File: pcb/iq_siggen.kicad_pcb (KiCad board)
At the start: 4 copper layers, 305 parts, among them J1 J3 - BANK0, J11 Conn_Coaxial, J12 Conn_01x01_Male, J13 Conn_01x01_Male, J14 Conn_01x01_Male, J15 Conn_01x01_Male, J16 Conn_01x01_Male, J17 Conn_01x01_Male, J18 Conn_Coaxial, J19 Conn_Coaxial, J2 J4 - BANK1, J3 Conn_01x10_Male, J4 Conn_01x01_Male, J5 Conn_01x10_Male, J6 Conn_Coaxial, J7 Conn_Coaxial, J8 Conn_Coaxial, J9 Conn_Coaxial, T1 Transformer_1P_SS, T2 Transformer_1P_SS, T3 Transformer_1P_SS, T4 Transformer_1P_SS, U1 AMS1117-3.3, U2 TPS72325DBVR, U3 TLV73325PDBVT, U4 TLV3542IDR, U5 LM2596S-ADJ, U6 MAX5853ETL-T, U7 TLV3542IDR

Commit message: routing mixer
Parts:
- moved D7 130.5 mm to (156.2, 257.8), turned to 180 degrees
- moved T1 122.7 mm to (150.5, 257.8), turned to 180 degrees
- moved T3 121.0 mm to (158.8, 250.2), turned to 90 degrees
- moved U4 120.3 mm to (127.6, 246.4)
- moved J12 120.0 mm to (76.8, 77.5)
- moved J17 118.8 mm to (64.8, 78.1)
- moved R25 111.3 mm to (260.3, 61.6)
- moved TP1 110.3 mm to (267.6, 63.1)
- moved J13 109.3 mm to (60.6, 70.5)
- moved J14 109.3 mm to (56.0, 70.5)
- moved J15 109.3 mm to (65.3, 70.5)
- moved D5 108.6 mm to (161.3, 257.8)
- moved R53 108.5 mm to (245.7, 56.5)
- moved U3 108.1 mm to (240.8, 57.6)
- moved R59 108.0 mm to (252.3, 59.1)
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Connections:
- T4 pad 1: GNDA -> /mixer/RF_I
- T4 pad 2: /mixer/RF_I -> GNDA
- T4 pad 3: Net-(D6-Pad3) -> Net-(D8-Pad3)
- T4 pad 5: Net-(D8-Pad3) -> Net-(D6-Pad3)
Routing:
- net Net-(D5-Pad2): track 0.00 -> 7.52 mm
- net Net-(D5-Pad1): track 0.00 -> 7.52 mm
- net Net-(D6-Pad2): track 0.00 -> 7.52 mm
- net Net-(D6-Pad1): track 0.00 -> 7.52 mm
- net Net-(D8-Pad3): track 0.00 -> 6.71 mm, vias 0 -> 1
- net Net-(D7-Pad3): track 0.00 -> 6.71 mm, vias 0 -> 1
- net Net-(D6-Pad3): track 0.00 -> 6.71 mm, vias 0 -> 1
- net Net-(D5-Pad3): track 0.00 -> 6.71 mm, vias 0 -> 1
- added copper zone on In1.Cu, net GNDA
- added copper zone on In2.Cu, net GNDA
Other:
- net class 100ohm differential added: clearance 0.1, trace_width 0.117094, via_dia 0.8, via_drill 0.4
- net class 50ohm single ended added: clearance 0.1, trace_width 0.146812, via_dia 0.8, via_drill 0.4
- net class Default: clearance 0.2 -> 0.1
- rule trace_clearance: 0.2 -> 0.1
- rule trace_min: 0.13 -> 0.1
- rule via_min_drill: 0.25 -> 0.23

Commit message: lined up data bus resistors, done 5v reg, started the -5V switching regulator
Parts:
- moved R65 202.3 mm to (181.0, 245.3), turned to 270 degrees
- moved R64 196.4 mm to (176.7, 244.5)
- moved C1 195.2 mm to (187.3, 244.5)
- moved R60 194.8 mm to (167.0, 248.3), turned to 270 degrees
- moved R62 190.0 mm to (171.6, 242.6), turned to 180 degrees
- moved R24 176.4 mm to (91.4, 83.2), turned to 90 degrees
- moved R63 171.3 mm to (171.6, 247.0), turned to 180 degrees
- moved R61 169.7 mm to (167.0, 241.7), turned to 90 degrees
- moved R40 162.4 mm to (88.9, 83.2), turned to 270 degrees
- moved R38 158.7 mm to (99.1, 83.2), turned to 270 degrees
- moved J11 141.7 mm to (212.1, 244.7)
- moved R44 141.6 mm to (116.8, 83.4), turned to 270 degrees
- moved R23 141.1 mm to (94.0, 83.2), turned to 90 degrees
- moved R36 140.3 mm to (106.7, 83.2), turned to 270 degrees
- moved R22 139.8 mm to (96.5, 83.2), turned to 90 degrees
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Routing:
- net +3V3: track 0.00 -> 16.5 mm
- net +5V: track 0.00 -> 3.42 mm
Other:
- net class Default: trace_width 0.25 -> 0.1

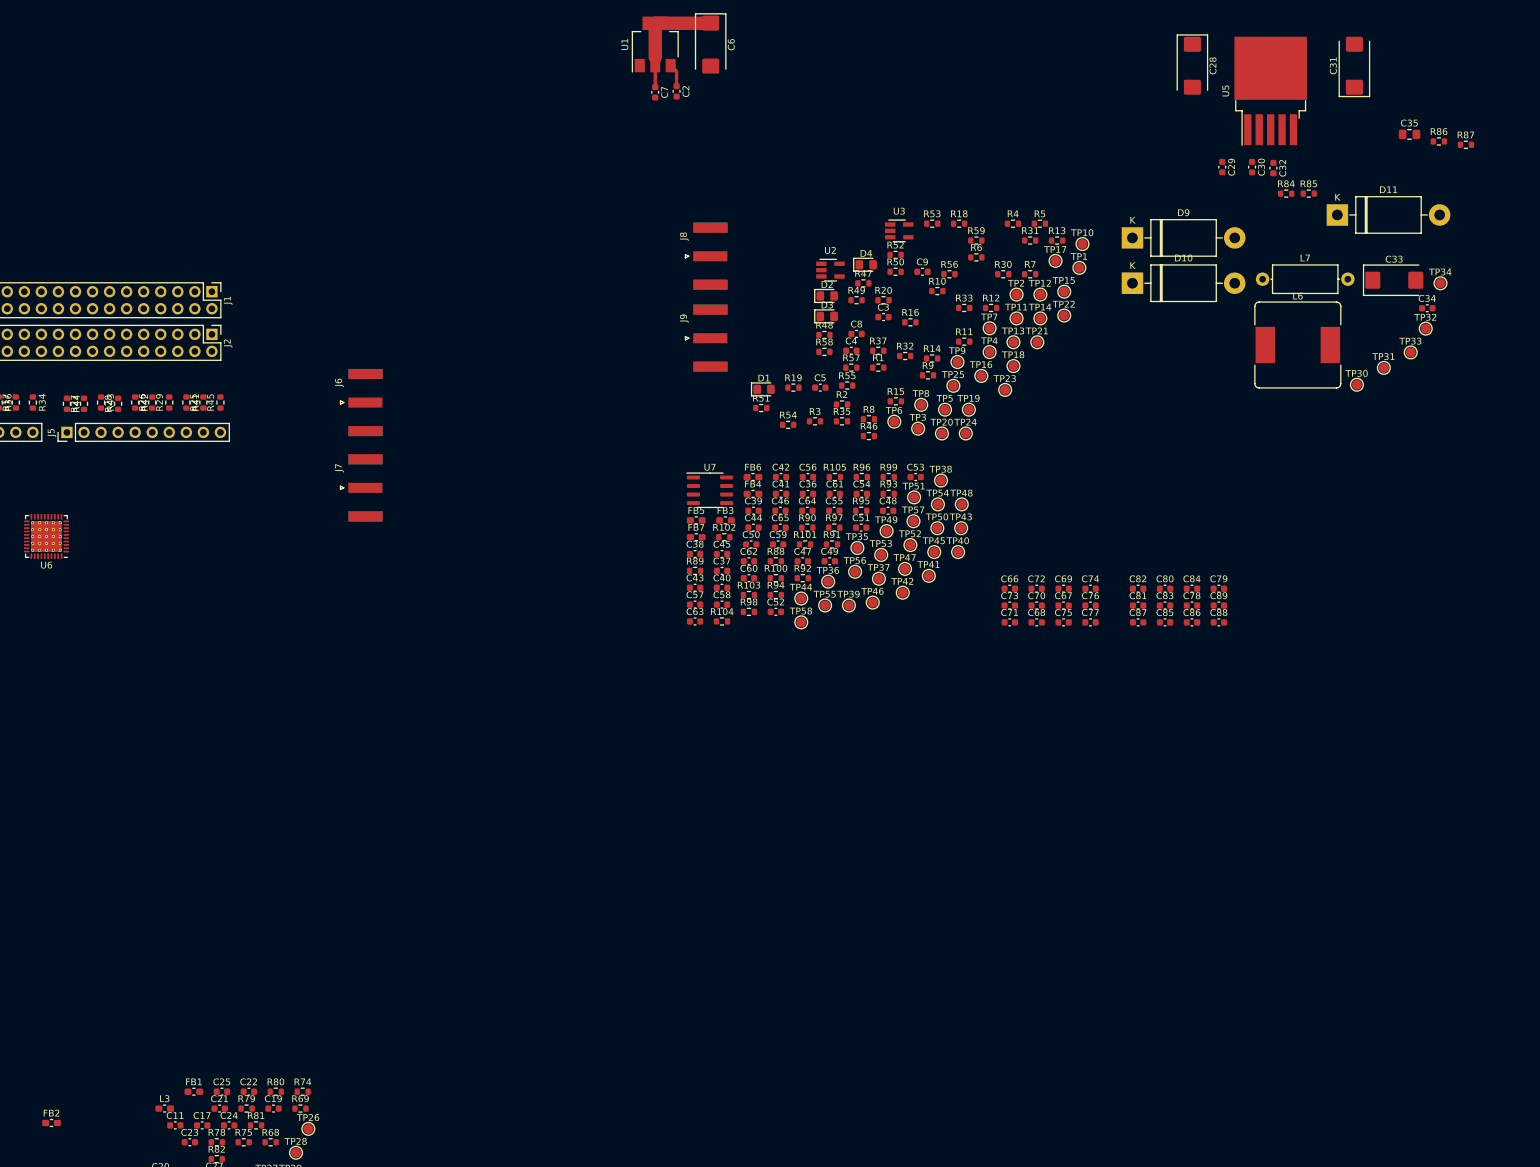
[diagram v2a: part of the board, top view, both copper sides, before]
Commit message: finish up vregs, routed filters, iq baseband outputs
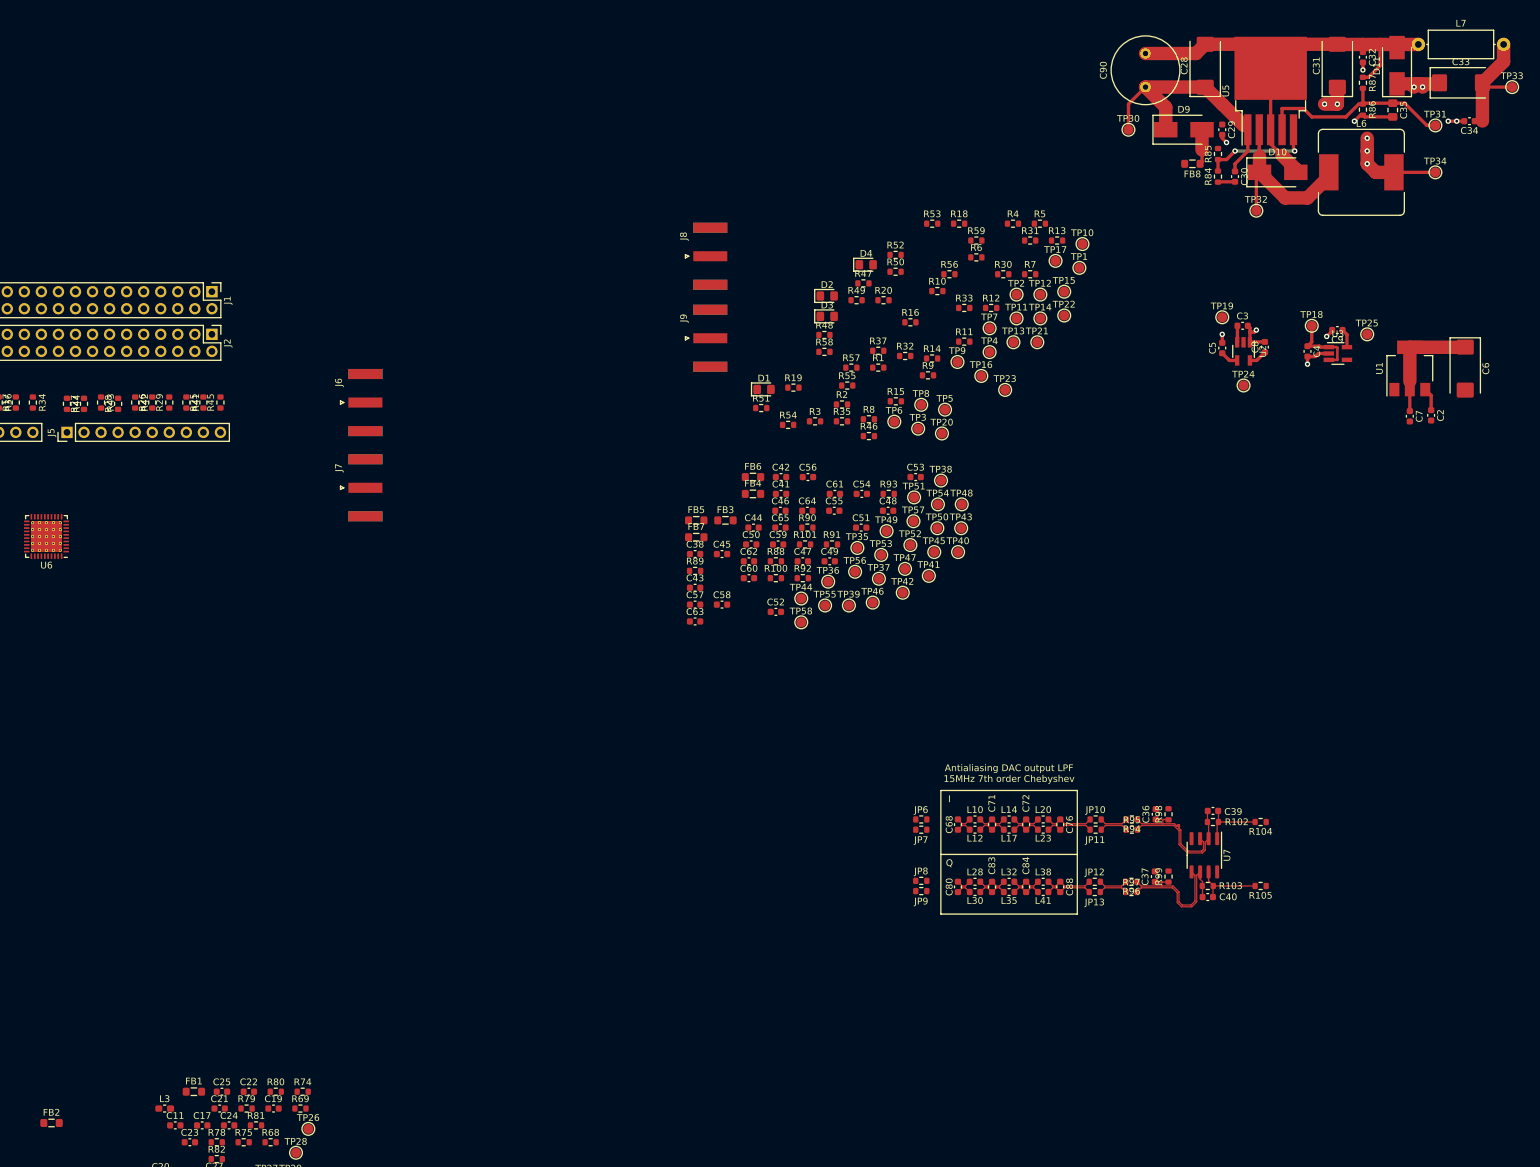
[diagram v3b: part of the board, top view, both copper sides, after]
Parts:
- removed C66, C67, C75, C77, C78, C79, C87, C89: 85p, Capacitor_SMD:C_0603_1608Metric
- removed C69, C70, C73, C74, C81, C82, C85, C86: 187p, Capacitor_SMD:C_0603_1608Metric
- added C90: 470u 50v electro, Capacitor_THT:C_Radial_D10.0mm_H20.0mm_P5.00mm, F.Cu at (277.5, 36.2)
- added FB8: Ferrite_Bead_Small, Inductor_SMD:L_0805_2012Metric_Pad1.05x1.20mm_HandSolder, F.Cu at (284.5, 47.6)
- added JP10: Jumper, Resistor_SMD:R_0603_1608Metric, F.Cu at (270.1, 145.3)
- added JP11: Jumper, Resistor_SMD:R_0603_1608Metric, F.Cu at (270.1, 146.8)
- added JP12: Jumper, Resistor_SMD:R_0603_1608Metric, F.Cu at (269.9, 154.6)
- added JP13: Jumper, Resistor_SMD:R_0603_1608Metric, F.Cu at (269.9, 156.1)
- added JP6: Jumper, Resistor_SMD:R_0603_1608Metric, F.Cu at (244.1, 145.3)
- added JP7: Jumper, Resistor_SMD:R_0603_1608Metric, F.Cu at (244.1, 146.8)
- added JP8: Jumper, Resistor_SMD:R_0603_1608Metric, F.Cu at (244.1, 154.4)
- added JP9: Jumper, Resistor_SMD:R_0603_1608Metric, F.Cu at (244.1, 156.0)
- added L10: 732n, Inductor_SMD:L_0603_1608Metric, F.Cu at (252.1, 145.3)
- added L12: 732n, Inductor_SMD:L_0603_1608Metric, F.Cu at (252.1, 146.8)
- added L14: 866n, Inductor_SMD:L_0603_1608Metric, F.Cu at (257.2, 145.3)
- added L17: 866n, Inductor_SMD:L_0603_1608Metric, F.Cu at (257.2, 146.8)
- added L20: 732n, Inductor_SMD:L_0603_1608Metric, F.Cu at (262.3, 145.3)
- added L23: 732n, Inductor_SMD:L_0603_1608Metric, F.Cu at (262.3, 146.8)
- added L28: 732n, Inductor_SMD:L_0603_1608Metric, F.Cu at (252.1, 154.6)
- added L30: 732n, Inductor_SMD:L_0603_1608Metric, F.Cu at (252.1, 156.1)
- added L32: 866n, Inductor_SMD:L_0603_1608Metric, F.Cu at (257.2, 154.6)
- added L35: 866n, Inductor_SMD:L_0603_1608Metric, F.Cu at (257.2, 156.1)
- added L38: 732n, Inductor_SMD:L_0603_1608Metric, F.Cu at (262.3, 154.6)
- added L41: 732n, Inductor_SMD:L_0603_1608Metric, F.Cu at (262.3, 156.1)
- C28: value 220u -> 100u 25V tantalum
- C31, C33: value 220u -> 220u tantalum 25V
- D10: value 1N5825 -> MBRS540T3G; footprint Diode_THT:D_DO-201AD_P15.24mm_Horizontal -> Diode_SMD:D_SMB_Handsoldering
- D11: value 1N5400 -> MBRS540T3G; footprint Diode_THT:D_DO-201AD_P15.24mm_Horizontal -> Diode_SMD:D_SMB_Handsoldering
- D9: value 1N5823 -> MBRS540T3G; footprint Diode_THT:D_DO-201AD_P15.24mm_Horizontal -> Diode_SMD:D_SMB_Handsoldering
- FB1, FB2, FB3, FB4, FB5, FB6, FB7: footprint Inductor_SMD:L_0603_1608Metric_Pad1.05x0.95mm_HandSolder -> Inductor_SMD:L_0805_2012Metric_Pad1.05x1.20mm_HandSolder
- moved C2 122.3 mm to (320.0, 85.1)
- moved C6 122.3 mm to (325.1, 78.1)
- moved C7 122.3 mm to (316.9, 85.2)
- moved U1 122.3 mm to (316.9, 78.1)
- moved U7 91.5 mm to (286.3, 150.6), turned to 270 degrees
- moved R105 87.9 mm to (294.6, 155.2), turned to 180 degrees
- moved C40 85.8 mm to (286.8, 156.8), turned to 180 degrees
- moved R104 85.6 mm to (294.6, 145.7), turned to 180 degrees
- moved R102 84.2 mm to (287.5, 145.7), turned to 180 degrees
- moved C39 81.7 mm to (287.5, 144.0), turned to 180 degrees
- moved R103 80.9 mm to (286.8, 155.2), turned to 180 degrees
- moved C37 78.9 mm to (278.9, 153.8), turned to 90 degrees
- moved R99 72.7 mm to (280.9, 153.8), turned to 90 degrees
- moved R96 72.4 mm to (275.4, 154.6), turned to 180 degrees
- moved C36 70.4 mm to (279.0, 144.5), turned to 90 degrees
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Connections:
- net Net-(C36-Pad1) renamed /IQ DAC and AA filter/I_FB_P
- net Net-(C37-Pad1) renamed /IQ DAC and AA filter/Q_FB_P
- net Net-(C39-Pad2) renamed /IQ DAC and AA filter/I_FB_N
- net Net-(C40-Pad2) renamed /IQ DAC and AA filter/Q_FB_N
- net Net-(JP10-Pad2) renamed /IQ DAC and AA filter/I_F_P
- net Net-(JP11-Pad2) renamed /IQ DAC and AA filter/I_F_N
- net Net-(JP12-Pad2) renamed /IQ DAC and AA filter/Q_F_P
- net Net-(JP13-Pad2) renamed /IQ DAC and AA filter/Q_F_N
- C28 pad 2: GNDA -> /negative rail generator/-5VO
- C31 pad 2: Net-(C31-Pad2) -> /negative rail generator/-5VO
- C32 pad 1: Net-(C31-Pad2) -> /negative rail generator/-5VO
- C71 pad 1: Net-(C69-Pad1) -> /IQ DAC and AA filter/I AA Filter/F_P
- C71 pad 2: Net-(C69-Pad2) -> /IQ DAC and AA filter/I AA Filter/F_N
- C72 pad 1: Net-(C72-Pad1) -> /IQ DAC and AA filter/I AA Filter/F2_P
- C72 pad 2: Net-(C72-Pad2) -> /IQ DAC and AA filter/I AA Filter/F2_N
- C83 pad 1: Net-(C81-Pad1) -> /IQ DAC and AA filter/Q AA filter/F_P
- C83 pad 2: Net-(C81-Pad2) -> /IQ DAC and AA filter/Q AA filter/F_N
- C84 pad 1: Net-(C84-Pad1) -> /IQ DAC and AA filter/Q AA filter/F2_P
- C84 pad 2: Net-(C84-Pad2) -> /IQ DAC and AA filter/Q AA filter/F2_N
- D10 pad 2: Net-(C31-Pad2) -> /negative rail generator/-5VO
- D11 pad 2: Net-(C31-Pad2) -> /negative rail generator/-5VO
- J1 pad 14: Net-(J1-Pad14) -> (no net)
- J1 pad 20: Net-(J1-Pad20) -> (no net)
- J1 pad 23: Net-(J1-Pad23) -> (no net)
- J1 pad 24: Net-(J1-Pad24) -> (no net)
- J1 pad 25: Net-(J1-Pad25) -> (no net)
- J1 pad 26: Net-(J1-Pad26) -> (no net)
- J1 pad 28: Net-(J1-Pad28) -> (no net)
- J1 pad 29: Net-(J1-Pad29) -> (no net)
- J1 pad 3: Net-(J1-Pad3) -> (no net)
- J1 pad 33: Net-(J1-Pad33) -> (no net)
- J1 pad 34: Net-(J1-Pad34) -> (no net)
- J1 pad 35: Net-(J1-Pad35) -> (no net)
- J1 pad 36: Net-(J1-Pad36) -> (no net)
- J1 pad 37: Net-(J1-Pad37) -> (no net)
- J1 pad 38: Net-(J1-Pad38) -> (no net)
- J1 pad 4: Net-(J1-Pad4) -> (no net)
- J1 pad 40: Net-(J1-Pad40) -> (no net)
- J1 pad 5: Net-(J1-Pad5) -> (no net)
- J1 pad 6: Net-(J1-Pad6) -> (no net)
- J1 pad 7: Net-(J1-Pad7) -> (no net)
- J1 pad 8: Net-(J1-Pad8) -> (no net)
- J18 pad 1: /mixer/LO_I_EXT -> (no net)
- J19 pad 1: /mixer/LO_Q_EXT -> (no net)
- J2 pad 13: Net-(J2-Pad13) -> (no net)
- J2 pad 18: Net-(J2-Pad18) -> (no net)
- J2 pad 23: Net-(J2-Pad23) -> (no net)
- J2 pad 36: Net-(J2-Pad36) -> (no net)
- J2 pad 40: Net-(J2-Pad40) -> (no net)
- J6 pad 1: /I_OUT -> (no net)
- J7 pad 1: /Q_OUT -> (no net)
- L7 pad 1: Net-(C31-Pad2) -> /negative rail generator/-5VO
- R85 pad 2: Net-(C31-Pad2) -> /negative rail generator/-5VO
- R87 pad 1: Net-(C31-Pad2) -> /negative rail generator/-5VO
- T1 pad 1: /mixer/LO_Q -> (no net)
- T2 pad 1: /mixer/LO_I -> (no net)
- U5 pad 3: Net-(C31-Pad2) -> /negative rail generator/-5VO
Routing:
- net /negative rail generator/-5VO: track 0.00 -> 70.6 mm
- net GNDA: track 0.00 -> 51.1 mm, vias 0 -> 16
- net Net-(C28-Pad1): track 0.00 -> 39.0 mm
- net Net-(C35-Pad1): track 0.00 -> 31.1 mm
- net Net-(D10-Pad1): track 0.00 -> 25.5 mm
- net -5V: track 0.00 -> 21.0 mm
- net /IQ DAC and AA filter/Q_FB_N: track 0.00 -> 20.1 mm
- net /IQ DAC and AA filter/I_FB_N: track 0.00 -> 19.6 mm
- net /IQ DAC and AA filter/Q_FB_P: track 0.00 -> 18.2 mm
- net /IQ DAC and AA filter/I_FB_P: track 0.00 -> 17.9 mm
- net Net-(R84-Pad2): track 0.00 -> 16.9 mm, vias 0 -> 2
- net +5V: track 3.42 -> 14.3 mm
- net Net-(C40-Pad1): track 0.00 -> 10.2 mm
- net Net-(C39-Pad1): track 0.00 -> 9.68 mm
- net /IQ DAC and AA filter/I AA Filter/50R_OUT_N: track 0.00 -> 7.25 mm
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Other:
- board text added: "Antialiasing DAC output LPF 15MHz 7th order Chebyshev"
- board text added: "I"
- board text added: "Q"

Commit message: layout progress
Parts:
- removed C47, C50: 0.1u, Capacitor_SMD:C_0603_1608Metric
- removed C90: 470u 50v electro, Capacitor_THT:C_Radial_D10.0mm_H20.0mm_P5.00mm
- removed R32, R33: DNI-50, Resistor_SMD:R_0603_1608Metric
- removed TP11, TP12, TP13, TP4, TP54, TP55: TestPoint, TestPoint:TestPoint_Pad_D1.5mm
- added J10: Barrel_Jack_MountingPin, Connector_BarrelJack:BarrelJack_Horizontal, F.Cu at (139.8, 89.5)
- added JP1: SolderJumper_3_Open, iq_siggen:50ohm_solder_jumper, F.Cu at (115.3, 120.2)
- added JP2: SolderJumper_3_Open, iq_siggen:50ohm_solder_jumper, F.Cu at (115.4, 134.0)
- C28: value 100u 25V tantalum -> 220u 25V tantalum
- J11, J18, J19, J6, J7, J8, J9: footprint Connector_Coaxial:SMA_Amphenol_132289_EdgeMount -> Connector_Coaxial:SMA_Samtec_SMA-J-P-X-ST-EM1_EdgeMount
- moved C2 203.5 mm to (117.0, 98.2)
- moved C6 203.5 mm to (122.0, 91.2)
- moved C7 203.5 mm to (113.8, 98.3)
- moved U1 203.5 mm to (113.8, 91.2)
- moved TP33 189.1 mm to (147.5, 77.0)
- moved R105 187.8 mm to (108.3, 131.7)
- moved R104 187.7 mm to (108.5, 122.2)
- moved C34 185.0 mm to (144.3, 77.0)
- moved C39 184.0 mm to (105.0, 120.5)
- moved R102 184.0 mm to (105.0, 122.2)
- moved R94 184.0 mm to (93.0, 121.8)
- moved R95 184.0 mm to (93.0, 123.3)
- moved C36 184.0 mm to (96.5, 121.0)
- moved C37 184.0 mm to (96.4, 130.3)
- moved C40 184.0 mm to (104.3, 133.3)
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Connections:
- J6 pad 1: (no net) -> /I_OUT
- J7 pad 1: (no net) -> /Q_OUT
- R14 pad 1: Net-(R14-Pad1) -> /mixer/CLK_I_N
- R30 pad 1: Net-(R14-Pad1) -> /mixer/CLK_I_N
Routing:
- net +5V: track 14.3 -> 65.0 mm, vias 0 -> 2
- net -5V: track 21.0 -> 38.3 mm
- net /negative rail generator/-5VO: track 70.6 -> 85.7 mm, vias 0 -> 2
- net GNDA: track 51.1 -> 66.1 mm, vias 16 -> 33
- net /IQ DAC and AA filter/+OPAMP_2.5V: track 0.00 -> 10.7 mm
- net /IQ DAC and AA filter/-OPAMP_2.5V: track 0.00 -> 10.5 mm
- net Net-(C28-Pad1): track 39.0 -> 28.9 mm
- net +2V5: track 2.81 -> 9.14 mm, vias 0 -> 2
- net Net-(R62-Pad1): track 0.00 -> 4.14 mm
- net Net-(C40-Pad1): track 10.2 -> 6.47 mm
- net /mixer/RF_I: track 0.00 -> 3.71 mm
- net Net-(C39-Pad1): track 9.68 -> 6.00 mm
- net /mixer/RF_Q: track 0.00 -> 3.68 mm
- net /IQ DAC and AA filter/Q_FB_P: track 18.2 -> 15.6 mm
- net /IQ DAC and AA filter/Q_FB_N: track 20.1 -> 18.0 mm
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- removed copper zone on In1.Cu, net GNDA
- removed copper zone on In2.Cu, net GNDA
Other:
- board outline added: 100 x 100 mm
- rule trace_min: 0.1 -> 0.0889
